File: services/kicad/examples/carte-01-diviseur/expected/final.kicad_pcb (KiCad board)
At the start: 2 copper layers, 25 x 20 mm, 5 parts, among them J1 IN

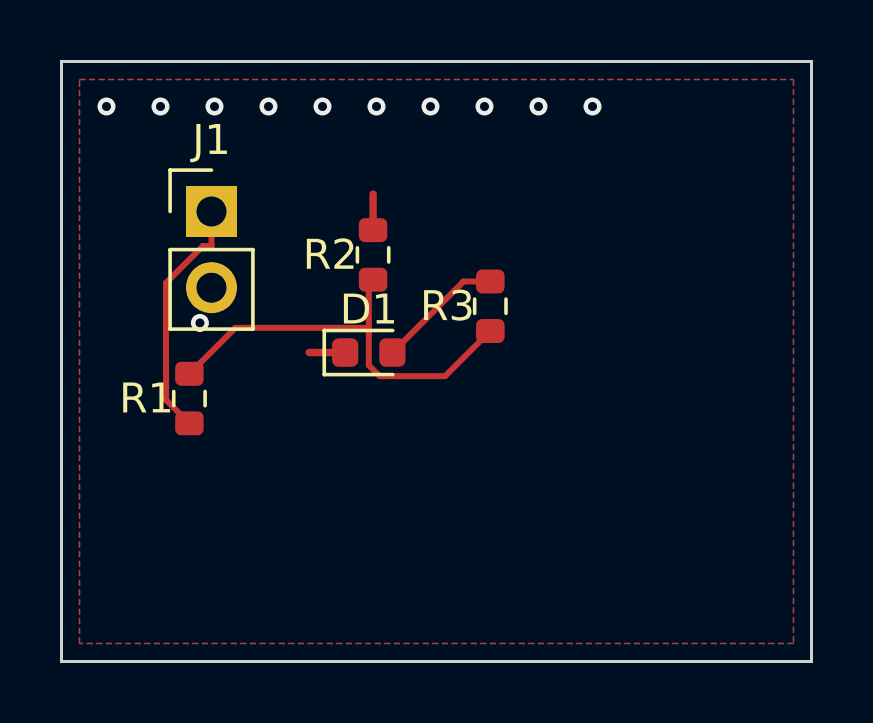
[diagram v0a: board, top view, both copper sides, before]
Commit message: feat(kicad): placement pro et routage 100 % fabricable sur les 16 cartes -- integration sur main (#164)
Branche d'integration coupee depuis origin/main (fab2a82, PR #162) : les
fichiers cles de main etaient des instantanes de feat/placement-seed-snap-
bypass (routing.py = 7981019, placement.py = 437a8b4...). On reprend donc
l'arbre entier de cette branche (345 commits, dernier 9f48667) et on y
conserve ce que main seul apportait :
- tools/verrou_routage.py + son test : « 6,2 Go par routage » rectifie
  (0,2 Go mesure ; c'est la concurrence qui emballe la memoire) ;
- tests/test_driver_llm_resync.py ;
- CLAUDE.md, PLAN.md, DECISIONS.md : fusion a trois voies, les sections
  des deux lignes conservees (2026-09-05 conteneur/verrou, 2026-09-07
  parcours asynchrone et chaine du driver, 2026-09-09/10 lecons).
Les skills *-delegate restent supprimes (remplaces le 2026-08-30).

Contenu : banc en deux phases (placement valide puis routage gele), snap
sur les regles natives, repli GND cible, journal Freerouting incremental,
horloge sans progres, via d'echappement vers le plan principal,
serigraphie degagee ; 16 cartes livrees a 100 %, 0 erreur DRC.

Verification : pytest services/kicad 1805 passed, 16 skipped ;
pnpm type-check 8/8.


Claude-Session: https://claude.ai/code/session_01TnMqm4La2CxQHHB5K8aSSV

Co-authored-by: Claude Fable 5.1 <noreply@anthropic.com>
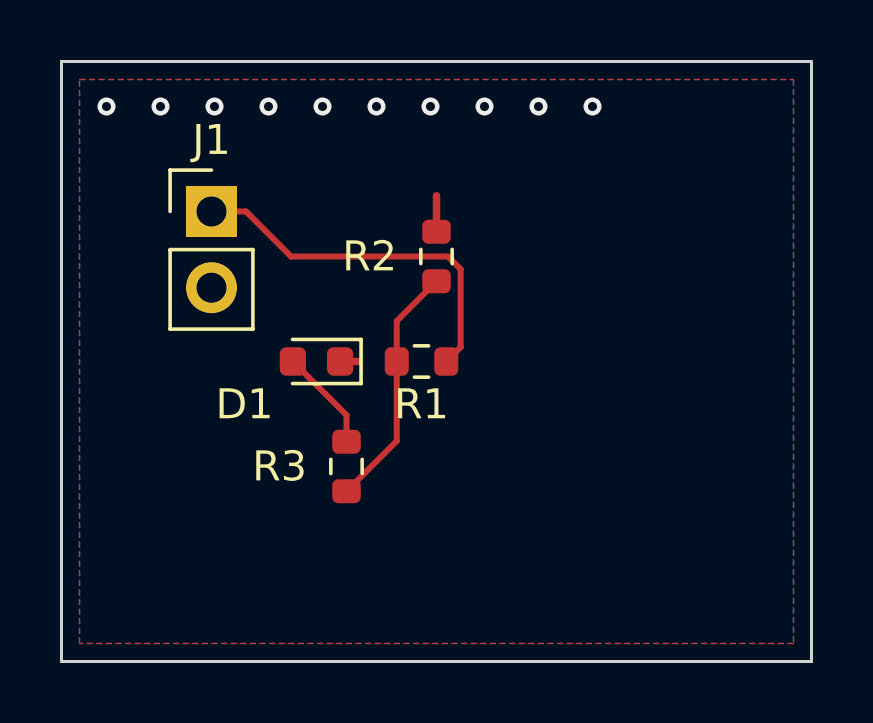
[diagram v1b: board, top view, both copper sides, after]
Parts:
- moved R1 7.83 mm to (148.0, 105.0), turned to 180 degrees
- moved R3 7.18 mm to (145.5, 108.5)
- moved R2 2.11 mm to (148.5, 101.5)
- moved D1 1.77 mm to (144.5, 105.0), turned to 180 degrees
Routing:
- net MID: track 14.4 -> 8.24 mm
- net VIN: track 8.18 -> 12.4 mm
- net LED_A: track 4.24 -> 3.42 mm
- net GND: track 2.40 -> 1.80 mm, vias 11 -> 10

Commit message: test(examples): quatre cartes livrées plus petites — contour resserré mesuré sur le banc (D-2026-09-13-c A)
Banc rejoué en taille heuristique (phase 1 puis phase 2 à placement gelé) :
carte-01 25x20 -> 24,8x17 (84 % de surface), carte-04 60x45 -> 45x44,8
(75 %), carte-06 80x60 -> 65,2x59,8 (81 %), carte-07 110x80 -> 99,5x79,8
(90 %) — toutes 100 % routées, 0 erreur DRC (vérifié en local), rendus 3D
régénérés. Gain nul sur les cartes denses (le génétique remplit la carte) ;
08 et 09 non livrées (dispersion du routage, surface inchangée) ; carte-11
non livrée (carte d'escalade). Tableau complet dans docs/DECISIONS.md.

Co-Authored-By: Claude Fable 5.1 <noreply@anthropic.com>
Claude-Session: https://claude.ai/code/session_01TnMqm4La2CxQHHB5K8aSSV
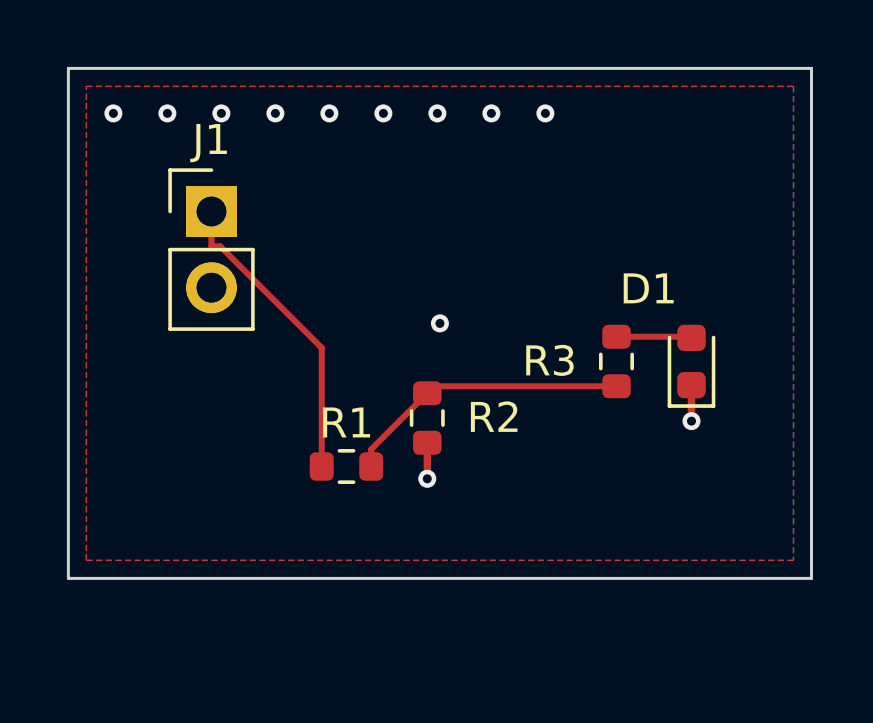
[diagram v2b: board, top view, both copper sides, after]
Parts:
- moved D1 12.5 mm to (157.0, 105.0), turned to 90 degrees
- moved R3 9.66 mm to (154.5, 105.0)
- moved R2 5.39 mm to (148.2, 106.9), turned to -90 degrees
- moved R1 4.30 mm to (145.5, 108.5), turned to 0 degrees
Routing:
- net VIN: track 12.4 -> 10.2 mm
- net MID: track 8.24 -> 9.62 mm
- net LED_A: track 3.42 -> 2.52 mm
- net GND: track 1.80 -> 2.40 mm, vias 10 -> 12
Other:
- board size 25 x 20 mm -> 24.8 x 17 mm

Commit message: chore(banc): relivrer carte-01..10 avec la couture corrigee
Boards reroutes par HTTP depuis placement.kicad_pcb inchange, avec le
code de #217. Juges par remesurer_banc.py : 0 erreur, 0 connexion
manquante sur les dix. 678 -> 443 vias ; la rangee de vias GND du bord
haut a disparu.

mesures.json : `board` recompte, `drc_du_board` rejuge, nouvelle cle
`couture_corrigee` (date, vias_avant, couches). journal.txt et les
champs du run d origine sont laisses tels quels et le disent.
rendu-3d.png : kicad-cli, modeles 3D, iso 1400x900.

Couches d un tirage : huit cartes sur 2, carte-08 et carte-10 sur 4.
CLAUDE.md et BANC_DRIVER_LLM.md recomptes. carte-11 non touchee.

Co-Authored-By: Claude Opus 5 (1M context) <noreply@anthropic.com>
Claude-Session: https://claude.ai/code/session_01TnMqm4La2CxQHHB5K8aSSV
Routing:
- net GND: vias 12 -> 2
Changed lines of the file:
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@@
-	)
-	(segment
-		(start 146.325 107.9271)
-		(end 146.325 108.5)
-		(width 0.2)
-		(layer "F.Cu")
-		(net "MID")
 	)
 	(segment
@@
 	)
 	(segment
-		(start 148.1929 107.7092)
-		(end 148.1929 108.9092)
+		(start 146.325 107.9271)
+		(end 146.325 108.5)
+		(width 0.2)
+		(layer "F.Cu")
+		(net "MID")
+	)
+	(segment
+		(start 157 105.7875)
+		(end 157 106.9875)
 		(width 0.25)
 		(layer "F.Cu")
@@
 	)
 	(segment
-		(start 157 105.7875)
-		(end 157 106.9875)
+		(start 148.1929 107.7092)
+		(end 148.1929 108.9092)
 		(width 0.25)
 		(layer "F.Cu")
@@
 	)
 	(via
-		(at 139.53 96.73)
-		(size 0.6)
-		(drill 0.3)
-		(layers "F.Cu" "B.Cu")
-		(net "GND")
-	)
-	(via
-		(at 137.73 96.73)
-		(size 0.6)
-		(drill 0.3)
-		(layers "F.Cu" "B.Cu")
-		(net "GND")
-	)
-	(via
-		(at 143.13 96.73)
-		(size 0.6)
-		(drill 0.3)
-		(layers "F.Cu" "B.Cu")
-		(net "GND")
-	)
-	(via
-		(at 148.615 103.73)
-		(size 0.6)
-		(drill 0.3)
-		(layers "F.Cu" "B.Cu")
-		(net "GND")
-	)
-	(via
-		(at 144.93 96.73)
-		(size 0.6)
-		(drill 0.3)
-		(layers "F.Cu" "B.Cu")
-		(net "GND")
-	)
-	(via
 		(at 157 106.9875)
 		(size 0.6)
@@
 		(net "GND")
 	)
-	(via
-		(at 150.33 96.73)
-		(size 0.6)
-		(drill 0.3)
-		(layers "F.Cu" "B.Cu")
-		(net "GND")
-	)
-	(via
-		(at 146.73 96.73)
-		(size 0.6)
-		(drill 0.3)
-		(layers "F.Cu" "B.Cu")
-		(net "GND")
-	)
-	(via
-		(at 152.13 96.73)
-		(size 0.6)
-		(drill 0.3)
-		(layers "F.Cu" "B.Cu")
-		(net "GND")
-	)
-	(via
-		(at 141.33 96.73)
-		(size 0.6)
-		(drill 0.3)
-		(layers "F.Cu" "B.Cu")
-		(net "GND")
-	)
-	(via
-		(at 148.53 96.73)
-		(size 0.6)
-		(drill 0.3)
-		(layers "F.Cu" "B.Cu")
-		(net "GND")
-	)
 	(segment
-		(start 154.5 104.175)
-		(end 156.9625 104.175)
+		(start 154.5375 104.2125)
+		(end 154.5 104.175)
 		(width 0.2)
 		(layer "F.Cu")
@@
 	)
 	(segment
-		(start 156.9625 104.175)
-		(end 157 104.2125)
+		(start 157 104.2125)
+		(end 154.5375 104.2125)
 		(width 0.2)
 		(layer "F.Cu")
 		(net "LED_A")
+	)
+	(segment
+		(start 144.675 108.5)
+		(end 144.675 104.5463)
+		(width 0.2)
+		(layer "F.Cu")
+		(net "VIN")
 	)
 	(segment
@@
 		(width 0.2)
 		(layer "F.Cu")
-		(net "VIN")
-	)
-	(segment
-		(start 144.675 108.5)
-		(end 144.675 104.5463)
-		(width 0.2)
-		(layer "F.Cu")

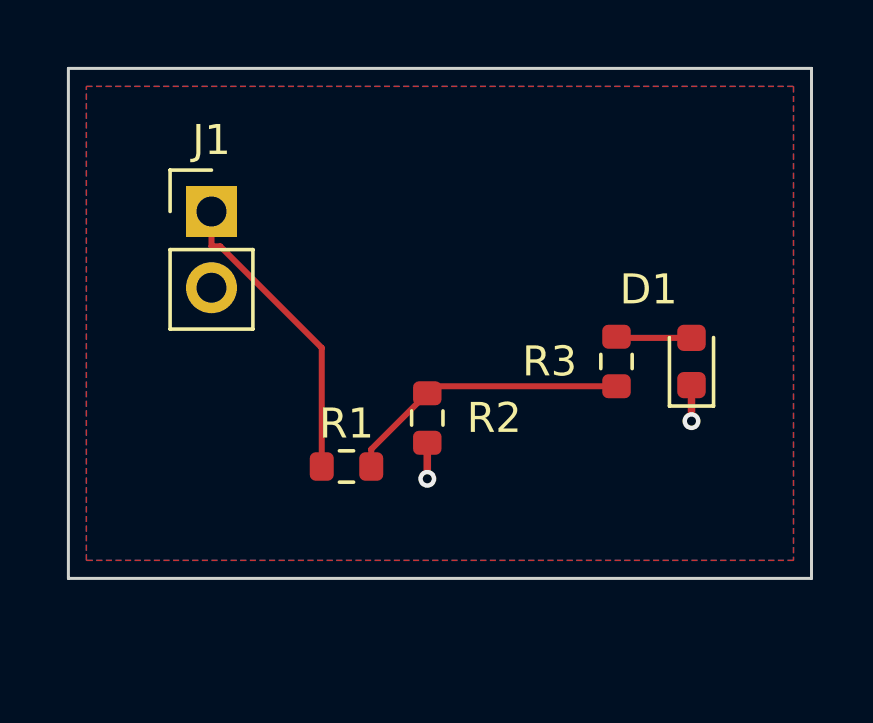
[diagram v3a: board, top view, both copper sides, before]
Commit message: chore(banc): relivrer carte-01/02/04/05 compactes (25 %, D-2026-09-20-a) (#222)
Chaine place -> route rejouee par HTTP sur les dix cartes avec le code de
#220/#221. Quatre sortent a 0 erreur et 0 connexion manquante, sur des
cartes 18 a 58 % plus petites :

  carte-01  24,8x17 -> 20x14      carte-02  55x40 -> 35x25
  carte-04  45x44,8 -> 39x30      carte-05  70x50 -> 46x33

placement.kicad_pcb et final.kicad_pcb remplaces ENSEMBLE ; mesures.json :
board recompte, drc_du_board rejuge (remesurer_banc.py), cle
carte_compacte (tailles et vias d avant, durees, moteur, pistes par
couche). Rendus refaits. Connecteurs a <= 5 mm d un bord (carte-02 J2 :
13,9 -> 3,8 mm) ; carte-05 J3 inchange a 11,4 mm (origine pin 1).

Les six autres gardent leur board du 2026-09-19 : 06 et 08 a 1 manquante,
03 et 07 mauvais, 09 et 10 sans board (tirages figes). Detail dans
BANC_DRIVER_LLM.md. carte-11 non touchee.


Claude-Session: https://claude.ai/code/session_01TnMqm4La2CxQHHB5K8aSSV

Co-authored-by: Claude Fable 5.1 <noreply@anthropic.com>
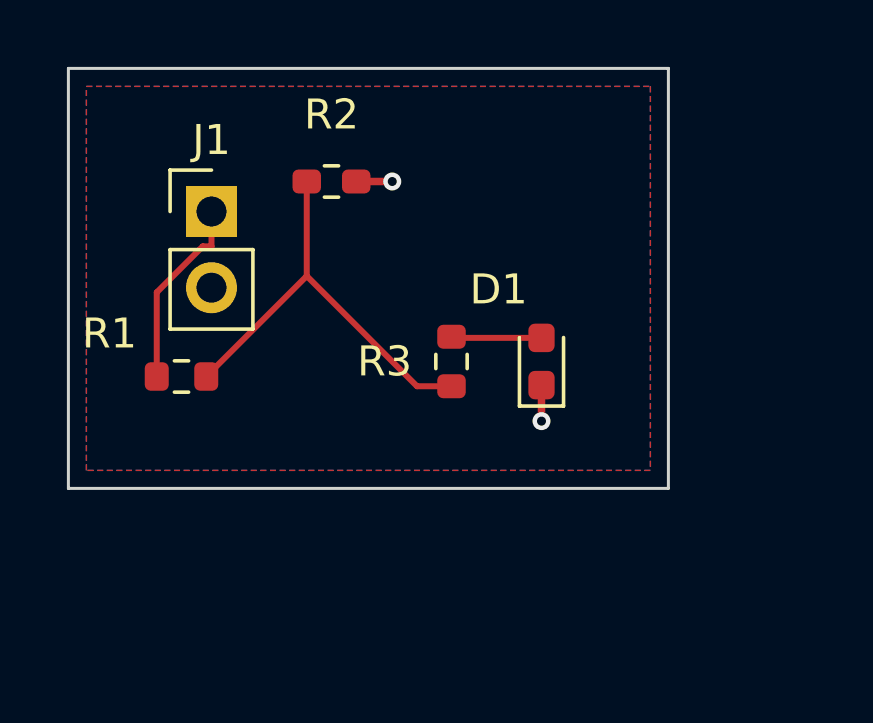
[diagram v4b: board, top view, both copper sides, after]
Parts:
- moved R2 8.51 mm to (145.0, 99.0), turned to 0 degrees
- moved R1 6.26 mm to (140.0, 105.5)
- moved R3 5.50 mm to (149.0, 105.0)
- moved D1 5.00 mm to (152.0, 105.0)
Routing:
- net MID: track 9.62 -> 14.2 mm
- net VIN: track 10.2 -> 6.43 mm
- net LED_A: track 2.52 -> 3.02 mm
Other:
- board size 24.8 x 17 mm -> 20 x 14 mm
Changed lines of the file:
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@@
 	(footprint "R_0603_1608Metric"
 		(layer "F.Cu")
-		(at 148.1929 106.8842 -90)
+		(at 145 99)
 		(descr "Resistor SMD 0603 (1608 Metric), square (rectangular) end terminal, IPC-7351 nominal, (Body size source: IPC-SM-782 page 72, https://www.pcb-3d.com/wordpress/wp-content/uploads/ipc-sm-782a_amendment_1_and_2.pdf)")
 		(tags "resistor")
@@
 		)
 		(property "Datasheet" ""
-			(at 0 0 270)
+			(at 0 0 0)
 			(layer "F.Fab")
 			(hide yes)
@@
 		)
 		(property "Description" ""
-			(at 0 0 270)
+			(at 0 0 0)
 			(layer "F.Fab")
 			(hide yes)
@@
 		(duplicate_pad_numbers_are_jumpers no)
 		(fp_line
+			(start -0.237258 -0.5225)
+			(end 0.237258 -0.5225)
+			(stroke
+				(width 0.12)
+				(type solid)
+			)
+			(layer "F.SilkS")
+		)
+		(fp_line
 			(start -0.237258 0.5225)
 			(end 0.237258 0.5225)
-			(stroke
-				(width 0.12)
-				(type solid)
-			)
-			(layer "F.SilkS")
-		)
-		(fp_line
-			(start -0.237258 -0.5225)
-			(end 0.237258 -0.5225)
 			(stroke
 				(width 0.12)
@@
 	(footprint "R_0603_1608Metric"
 		(layer "F.Cu")
-		(at 154.5 105 90)
+		(at 149 105 90)
 		(descr "Resistor SMD 0603 (1608 Metric), square (rectangular) end terminal, IPC-7351 nominal, (Body size source: IPC-SM-782 page 72, https://www.pcb-3d.com/wordpress/wp-content/uploads/ipc-sm-782a_amendment_1_and_2.pdf)")
 		(tags "resistor")
@@
 	(footprint "LED_0603_1608Metric"
 		(layer "F.Cu")
-		(at 157 105 90)
+		(at 152 105 90)
 		(descr "LED SMD 0603 (1608 Metric), square (rectangular) end terminal, IPC-7351 nominal, (Body size source: http://www.tortai-tech.com/upload/download/2011102023233369053.pdf)")
 		(tags "LED")
@@
 		)
 		(pad "1" smd roundrect
-			(at -0.7875 0 90)
+			(at -0.7875 0 180)
 			(size 0.875 0.95)
 			(layers "F.Cu" "F.Mask" "F.Paste")
@@
 		)
 		(pad "2" smd roundrect
-			(at 0.7875 0 90)
+			(at 0.7875 0 180)
 			(size 0.875 0.95)
 			(layers "F.Cu" "F.Mask" "F.Paste")
@@
 	(footprint "R_0603_1608Metric"
 		(layer "F.Cu")
-		(at 145.5 108.5)
+		(at 140 105.5)
 		(descr "Resistor SMD 0603 (1608 Metric), square (rectangular) end terminal, IPC-7351 nominal, (Body size source: IPC-SM-782 page 72, https://www.pcb-3d.com/wordpress/wp-content/uploads/ipc-sm-782a_amendment_1_and_2.pdf)")
 		(tags "resistor")
 		(property "Reference" "R1"
-			(at 0 -1.43 0)
+			(at -2.4 -1.43 0)
 			(layer "F.SilkS")
 			(effects
@@
 	(gr_rect
 		(start 136.23 95.23)
-		(end 161 112.23)
+		(end 156.23 109.23)
 		(stroke
 			(width 0.1)
@@
 	)
 	(segment
-		(start 148.1929 106.0592)
-		(end 146.325 107.9271)
+		(start 147.85 105.825)
+		(end 144.175 102.15)
 		(width 0.2)
 		(layer "F.Cu")
@@
 	)
 	(segment
-		(start 148.4271 105.825)
-		(end 148.1929 106.0592)
+		(start 144.175 99)
+		(end 144.175 102.15)
 		(width 0.2)
 		(layer "F.Cu")
@@
 	)
 	(segment
-		(start 154.5 105.825)
-		(end 148.4271 105.825)
+		(start 149 105.825)
+		(end 147.85 105.825)
 		(width 0.2)
 		(layer "F.Cu")
@@
 	)
 	(segment
-		(start 146.325 107.9271)
-		(end 146.325 108.5)
+		(start 144.175 102.15)
+		(end 140.825 105.5)
 		(width 0.2)
 		(layer "F.Cu")
@@
 	)
 	(segment
-		(start 157 105.7875)
-		(end 157 106.9875)
+		(start 152 105.7875)
+		(end 152 106.9875)
 		(width 0.25)
 		(layer "F.Cu")
@@
 	)
 	(segment
-		(start 148.1929 107.7092)
-		(end 148.1929 108.9092)
+		(start 145.825 99)
+		(end 147.025 99)
 		(width 0.25)
 		(layer "F.Cu")
@@
 	)
 	(via
-		(at 148.1929 108.9092)
+		(at 152 106.9875)
 		(size 0.6)
 		(drill 0.3)
@@
 	)
 	(via
-		(at 157 106.9875)
+		(at 147.025 99)
 		(size 0.6)
 		(drill 0.3)
@@
 	)
 	(segment
-		(start 154.5375 104.2125)
-		(end 154.5 104.175)
+		(start 149.0375 104.2125)
+		(end 149 104.175)
 		(width 0.2)
 		(layer "F.Cu")
@@
 	)
 	(segment
-		(start 157 104.2125)
-		(end 154.5375 104.2125)
+		(start 152 104.2125)
+		(end 149.0375 104.2125)
 		(width 0.2)
 		(layer "F.Cu")
@@
 	)
 	(segment
-		(start 144.675 108.5)
-		(end 144.675 104.5463)
-		(width 0.2)
-		(layer "F.Cu")
-		(net "VIN")
-	)
-	(segment
-		(start 141.2904 101.1617)
-		(end 141 101.1617)
+		(start 139.175 102.6963)
+		(end 139.175 105.5)
 		(width 0.2)
 		(layer "F.Cu")
@@
 	)
 	(segment
-		(start 144.675 104.5463)
-		(end 141.2904 101.1617)
+		(start 141 101.1617)
+		(end 140.7096 101.1617)
+		(width 0.2)
+		(layer "F.Cu")
+		(net "VIN")
+	)
+	(segment
+		(start 140.7096 101.1617)
+		(end 139.175 102.6963)
 		(width 0.2)
 		(layer "F.Cu")
@@
 		(polygon
 			(pts
-				(xy 136.83 95.83) (xy 160.4 95.83) (xy 160.4 111.63) (xy 136.83 111.63)
+				(xy 136.83 95.83) (xy 155.63 95.83) (xy 155.63 108.63) (xy 136.83 108.63)
 			)
 		)
@@
 		(polygon
 			(pts
-				(xy 136.83 95.83) (xy 160.4 95.83) (xy 160.4 111.63) (xy 136.83 111.63)
-			)
-		)
+				(xy 136.83 95.83) (xy 155.63 95.83) (xy 155.63 108.63) (xy 136.83 108.63)
+			)
+		)

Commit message: fix(banc): le contour n etait JAMAIS resserre — dix cartes divisees par 2 a 4
Question de l utilisateur devant les rendus : « tu es satisfait de ce
placement ? ». Non, et la mesure lui donnait raison.

    carte-10 livree     140 x 105 mm = 14725 mm2
    son circuit          51 x  66 mm =  3366 mm2
    OCCUPATION                            23 %
    connecteurs                      56 a 75 mm du circuit
    fil de signal                      1230 mm  (VIN a lui seul 112 mm)

LA CAUSE : `run_pipeline.py` n envoyait pas `auto_size_board` a `/place/auto`.
Le resserrement du contour sur le placement existe depuis le 2026-09-13 et ne
s execute que si l appelant l autorise ; le defaut du modele est `False`.

C est le SEPTIEME levier de ce projet qui existe et que personne n appelle,
apres max_distance_mm, anchor_pin, WorkflowConfig.grid, constraints,
move_reference, bottom_up_placement et LocalRerouter.

⚠️ Et il etait INVISIBLE : la chaine de PRODUCTION passe bien le drapeau depuis
`handlePlacement`. Le banc mesurait donc un comportement que le produit n a
pas — l inverse exact de ce a quoi sert un banc.

MESURE APRES CORRECTION, meme circuit, meme graine :

    carte             demandee      REELLE        err  manq
    carte-01           25 x 20     20,1 x 14,6     0    0
    carte-02           55 x 40     34,9 x 25,4     0    0
    carte-03           50 x 35     26,1 x 20,1     0    0
    carte-04           60 x 45     36,6 x 27,2     0    0
    carte-05           70 x 50     43,6 x 32,6     0    0
    carte-06           80 x 60     48,5 x 36,4     0    0
    carte-07          110 x 80     53,2 x 38,8     0    0
    carte-08          125 x 95     56,4 x 44,1     0    0
    carte-09          130 x 100    57,3 x 45,2     0    0
    carte-10          140 x 105    61,0 x 45,8     0    0

Dix sur dix, 100 % route, aucune erreur, aucune connexion manquante. Sur
carte-10 : occupation 23 -> 56 %, fil de signal 1230 -> 652 mm, VIN 112 -> 45,5,
connecteurs 56-75 -> 23-35 mm.

ET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
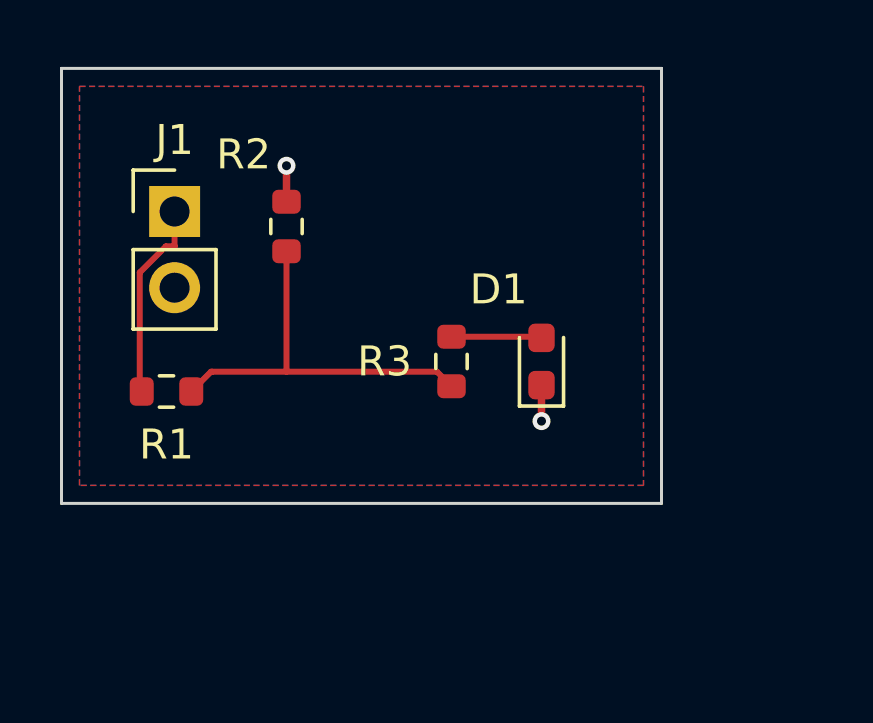
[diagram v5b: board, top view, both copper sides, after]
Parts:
- moved R2 2.12 mm to (143.5, 100.5), turned to 90 degrees
- moved J1 1.23 mm to (139.8, 100.0)
- moved R1 0.71 mm to (139.5, 106.0)
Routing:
- net MID: track 14.2 -> 13.2 mm
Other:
- board size 20 x 14 mm -> 20 x 14.5 mm
